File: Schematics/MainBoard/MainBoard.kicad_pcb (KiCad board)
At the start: 6 copper layers, 299.7 x 299.7 mm, 200 parts, among them J1 Barrel_Jack, J10 ALU Result LED Connector, J11 Address Bus LED Connector, J12 Data Bus LED Connector, J13 PC/IF Connector [0..7], J14 PC/IF Connector [8..15], J15 IROM Connector [0..7], J16 IROM Connector [8..15], J2 Device Select LED Connector, J3 Program Counter LED Connector, J4 Instruction Register LED Conn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, J5 C Register LED Connector, J6 Control Word LED Connector, J7 Speed Control LED Connector, J8 A Register LED Connector, J9 B Register LED Connector, SW1 Step, SW2 Reset, U1 74LS393, U10 IDT71256SA12TPG, U11 IDT71256SA12TPG, U12 74F377, U13 74LS138, U14 74F377, U15 74F377, U16 74LS245, U17 74LS245, U18 74F161, U19 74F161, U2 74LS32, U20 74F161, U21 74F161, U22 74F574, U23 74F574, U26 74F157, U27 74F157, U28 74F157, U29 74F157, U3 74F377, U30 74LS08, U31 74LS04, U32 74LS32, U33 IDT71256SA12TPG, U34 IDT71256SA12TPG, U35 74LS245, U36 74LS245, U37 74F157, U38 74F157, U39 74F574, U4 74LS139, U40 74F157, U41 74F157, U42 74F574, U43 GLS29EE010, U44 GLS29EE010, U45 74F574, U46 74F574, U47 74F574, U48 74LS245, U49 LM393, U5 74LS245, U50 LM393, U51 GLS29EE010, U52 LM393, U53 LM393, U54 74LS04, U55 LM555, U56 74LS393, U57 74LS151, U58 74LS393, U59 74LS393, U6 GLS29EE010, U60 LM555, U61 MCP100-450D, U62 74LS04, U63 74LS08, U64 74LS157, U65 74F377, U66 74LS245, U67 74F377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

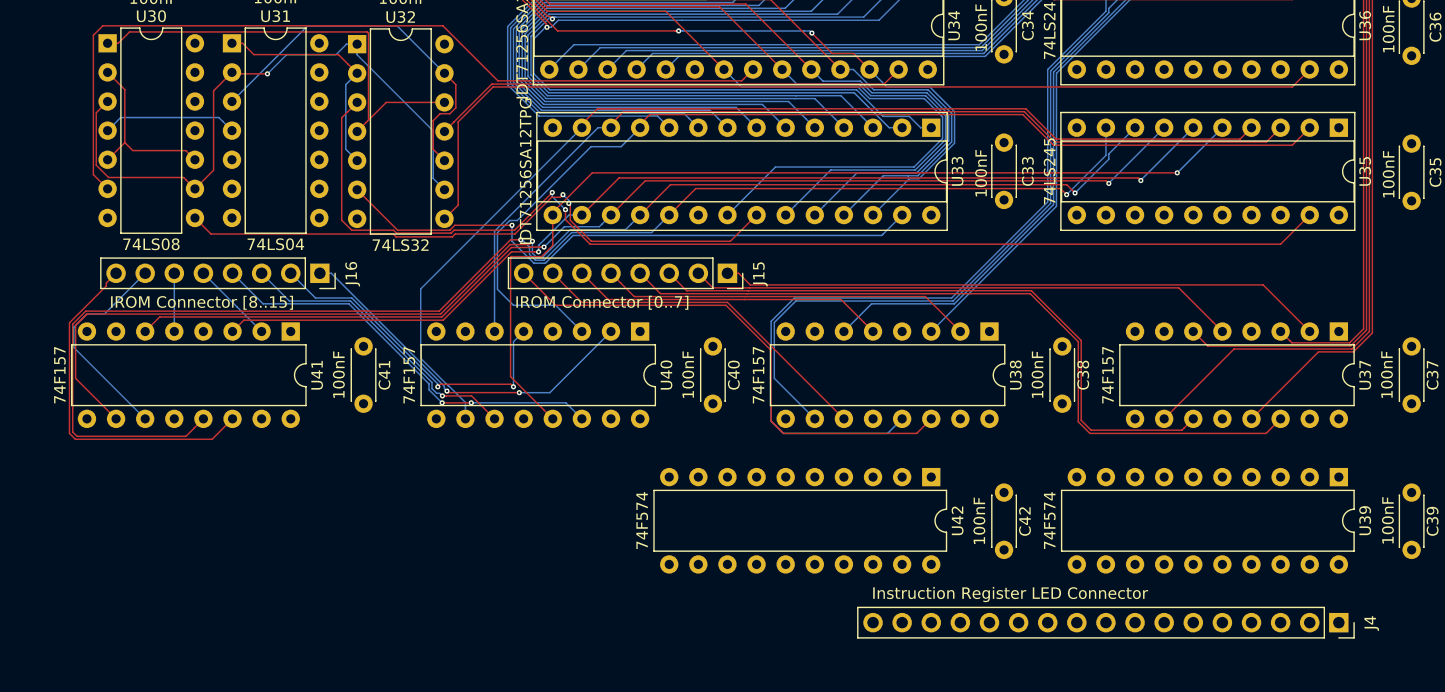
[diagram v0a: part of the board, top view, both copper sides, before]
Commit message: checkpoint: route up through the Instruction Register
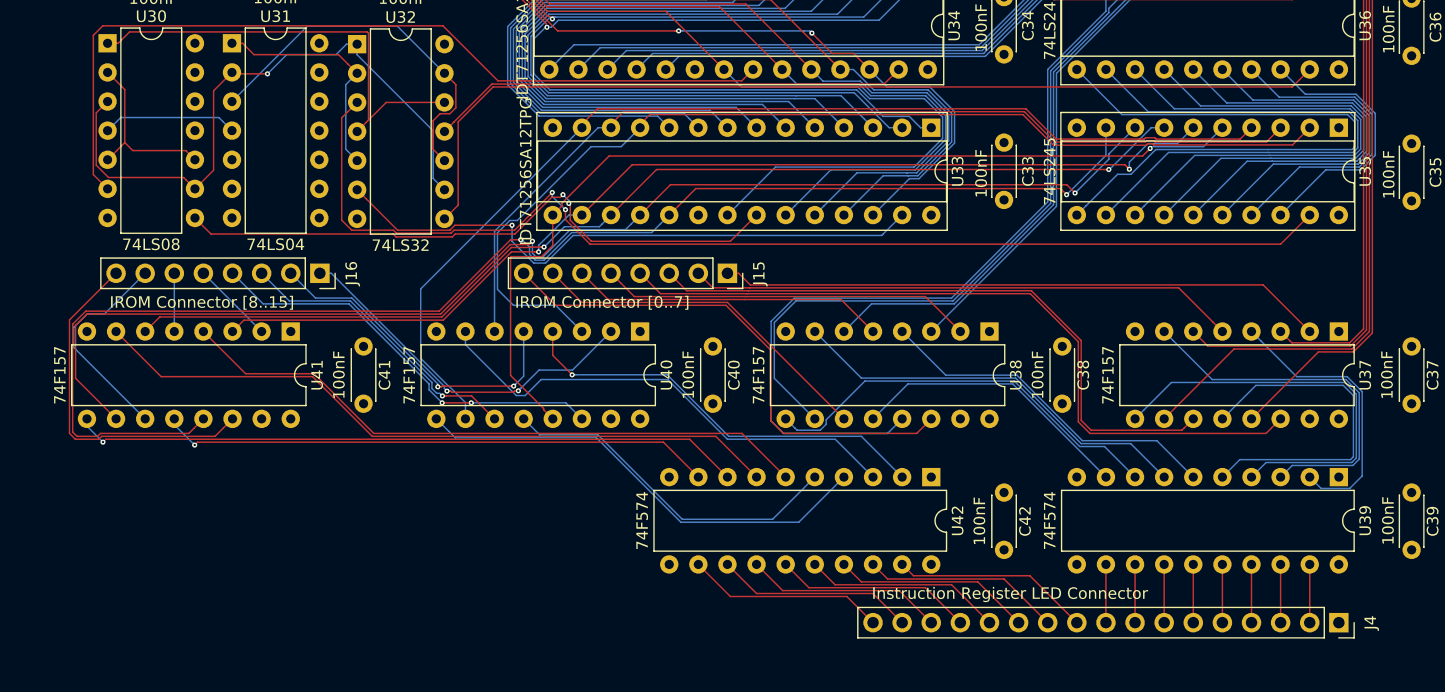
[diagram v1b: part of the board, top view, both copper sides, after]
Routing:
- net Net-(U41-Pad7): track 0.00 -> 61.1 mm
- net Net-(U41-Pad9): track 0.00 -> 58.6 mm, vias 0 -> 1
- net Net-(U41-Pad4): track 0.00 -> 56.1 mm
- net DataBus7: track 0.00 -> 55.0 mm
- net DataBus6: track 0.00 -> 50.6 mm
- net Net-(U41-Pad12): track 0.00 -> 48.3 mm, vias 0 -> 1
- net DataBus5: track 0.00 -> 46.1 mm
- net Net-(U40-Pad7): track 0.00 -> 42.6 mm
- net DataBus4: track 0.00 -> 41.7 mm
- net Net-(U40-Pad9): track 0.00 -> 40.9 mm
- net DataBus3: track 0.00 -> 37.2 mm
- net Net-(U40-Pad4): track 0.00 -> 37.0 mm, vias 0 -> 1
- net Net-(U37-Pad9): track 0.00 -> 36.4 mm
- net Net-(U38-Pad9): track 0.00 -> 36.4 mm
- net Net-(U38-Pad7): track 0.00 -> 35.7 mm
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
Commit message: stake out a place for the Program Counter ICs.
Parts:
- moved J3 325.3 mm to (309.9, 109.2), turned to 270 degrees
- moved U18 312.3 mm to (309.9, 96.5), turned to 270 degrees
- moved U19 299.0 mm to (279.4, 96.5), turned to 270 degrees
- moved C18 293.2 mm to (316.2, 97.8), turned to 270 degrees
- moved U20 291.0 mm to (248.9, 96.5), turned to 270 degrees
- moved U21 288.8 mm to (218.4, 96.5), turned to 270 degrees
- moved C19 279.7 mm to (285.8, 97.8), turned to 270 degrees
- moved C21 275.6 mm to (224.8, 102.9), turned to 90 degrees
- moved C20 274.3 mm to (255.3, 97.8), turned to 270 degrees

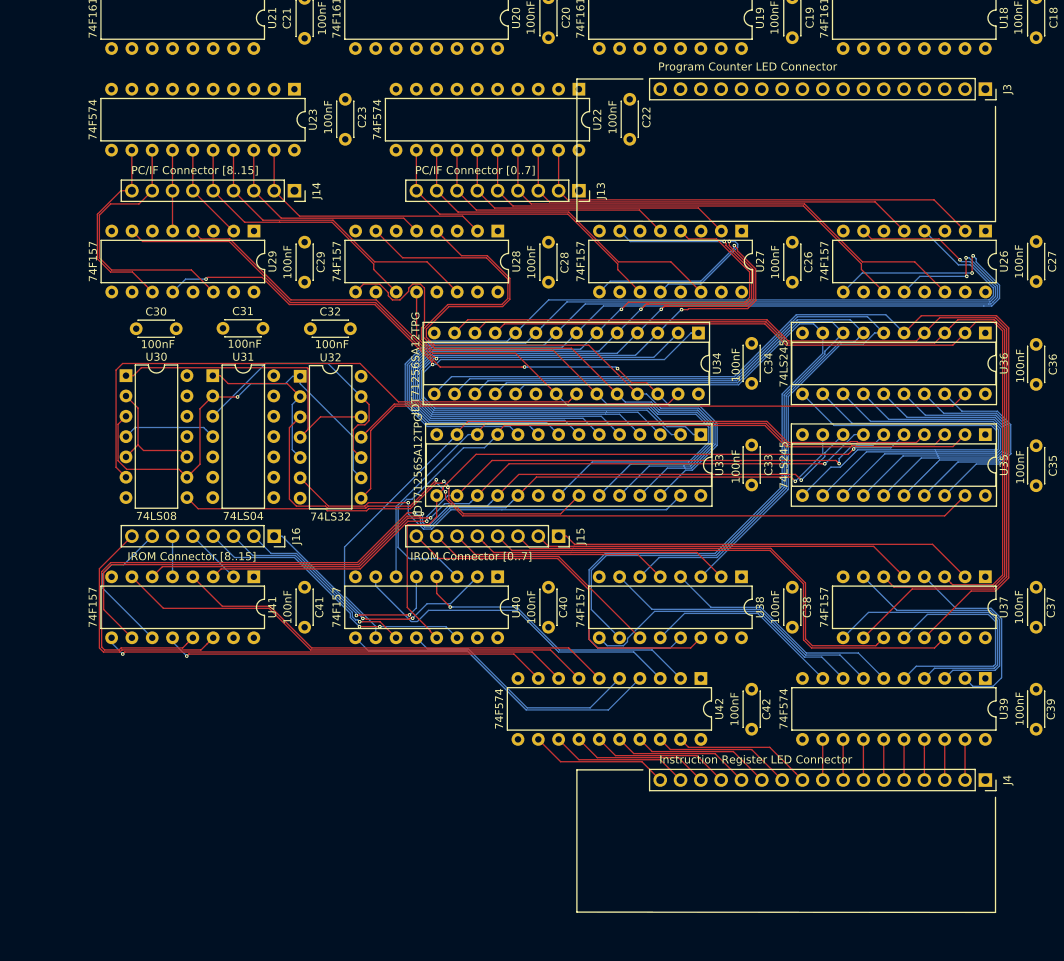
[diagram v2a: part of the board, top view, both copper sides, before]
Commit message: Route connection between PC and PC/IF.
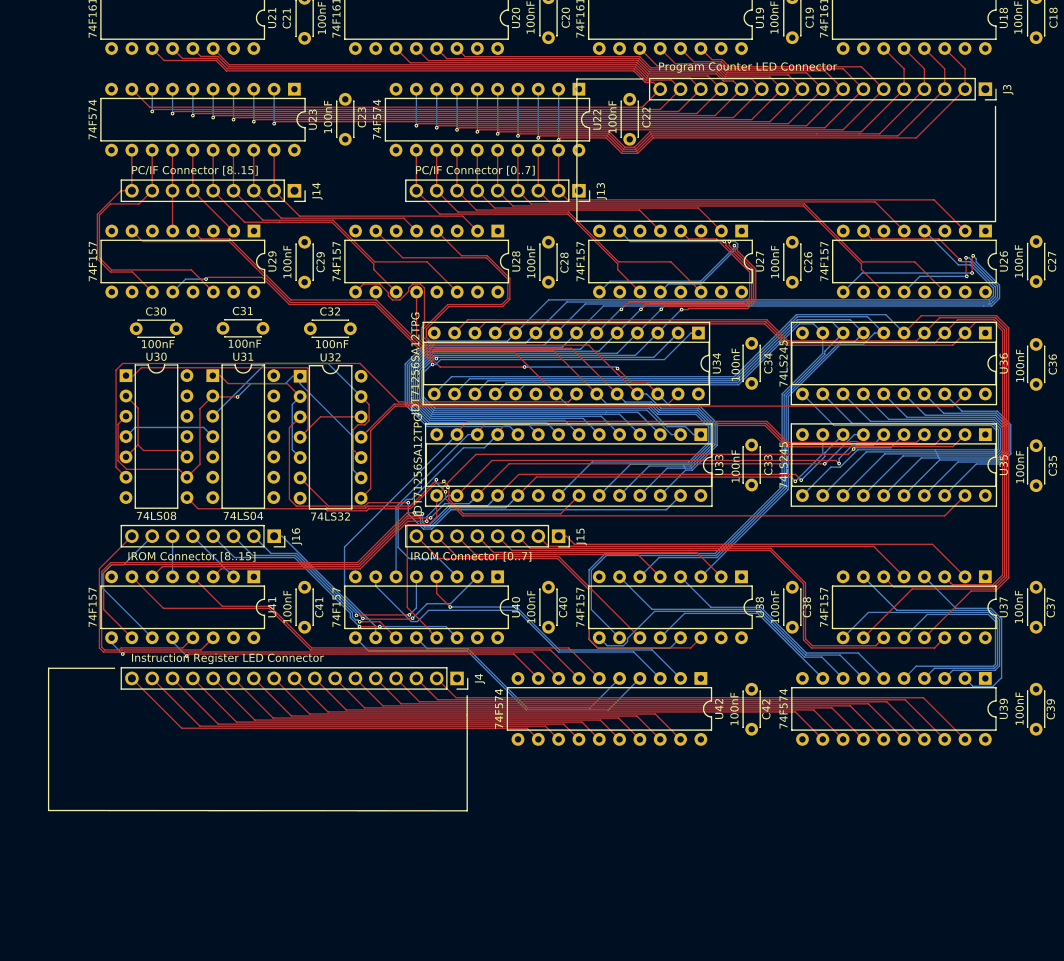
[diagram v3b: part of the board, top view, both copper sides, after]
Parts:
- moved J4 67.3 mm to (243.8, 182.9)
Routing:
- net PC12: track 0.00 -> 136.3 mm, vias 0 -> 1
- net PC13: track 0.00 -> 136.0 mm, vias 0 -> 1
- net PC14: track 0.00 -> 135.6 mm, vias 0 -> 1
- net PC15: track 0.00 -> 133.5 mm
- net PC8: track 0.00 -> 117.4 mm, vias 0 -> 1
- net PC9: track 0.00 -> 117.1 mm, vias 0 -> 1
- net PC10: track 0.00 -> 116.7 mm, vias 0 -> 1
- net PC11: track 0.00 -> 116.3 mm, vias 0 -> 1
- net PC4: track 0.00 -> 83.3 mm, vias 0 -> 1
- net PC5: track 0.00 -> 82.9 mm, vias 0 -> 1
- net PC6: track 0.00 -> 82.6 mm, vias 0 -> 1
- net PC7: track 0.00 -> 82.2 mm, vias 0 -> 1
- net PC0: track 0.00 -> 67.5 mm, vias 0 -> 1
- net PC1: track 0.00 -> 67.1 mm, vias 0 -> 1
- net PC2: track 0.00 -> 66.8 mm, vias 0 -> 1
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
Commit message: Stake out positions for the X and Y registers.
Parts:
- moved J11 319.2 mm to (243.8, 91.4), turned to 270 degrees
- moved C15 304.0 mm to (280.7, 85.1), turned to 270 degrees
- moved U15 300.2 mm to (274.3, 83.8), turned to 270 degrees
- moved U17 297.5 mm to (287.0, 91.4), turned to 90 degrees
- moved C14 295.5 mm to (280.7, 72.4), turned to 270 degrees
- moved U14 292.3 mm to (274.3, 71.1), turned to 270 degrees
- moved U16 288.1 mm to (287.0, 78.7), turned to 90 degrees
- moved C17 285.6 mm to (316.2, 85.1), turned to 270 degrees
- moved C16 276.8 mm to (316.2, 72.4), turned to 270 degrees
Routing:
- net ~J: track 0.00 -> 94.0 mm
- net Net-(U20-Pad15): track 0.00 -> 44.3 mm
- net Net-(U18-Pad15): track 0.00 -> 44.3 mm

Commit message: Stake out positions for register D and Device Select.
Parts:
- moved J2 265.2 mm to (243.8, 71.1), turned to 270 degrees
- moved C13 250.6 mm to (280.7, 64.8), turned to 90 degrees
- moved U13 242.7 mm to (274.3, 58.4), turned to 270 degrees
- moved U12 228.0 mm to (309.9, 58.4), turned to 270 degrees
- moved C12 211.0 mm to (316.2, 64.8), turned to 90 degrees

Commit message: Add M3 mounting holes (grounded) at all four corners of the board.
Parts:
- added REF**: MountingHole_3.2mm_M3_Pad, MountingHole:MountingHole_3.2mm_M3_Pad, F.Cu at (142.2, 45.7)
- added REF**: MountingHole_3.2mm_M3_Pad, MountingHole:MountingHole_3.2mm_M3_Pad, F.Cu at (142.2, 335.3)
- added REF**: MountingHole_3.2mm_M3_Pad, MountingHole:MountingHole_3.2mm_M3_Pad, F.Cu at (431.8, 335.3)
- added REF**: MountingHole_3.2mm_M3_Pad, MountingHole:MountingHole_3.2mm_M3_Pad, F.Cu at (431.8, 45.7)
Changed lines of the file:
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@@
     (tracks 1412)
     (zones 0)
-    (modules 200)
+    (modules 204)
     (nets 306)
   )
@@
     (mod_text_size 1 1)
     (mod_text_width 0.15)
-    (pad_size 1.524 1.524)
-    (pad_drill 0.762)
+    (pad_size 6.4 6.4)
+    (pad_drill 3.200001)
     (pad_to_mask_clearance 0)
     (aux_axis_origin 0 0)
@@
     (add_net ~YO)
   )
+  (module MountingHole:MountingHole_3.2mm_M3_Pad locked (layer F.Cu)
+    (at 142.24 45.72)
+    (descr "Mounting Hole 3.2mm, M3")
+    (tags "mounting hole 3.2mm m3")
+    (attr virtual)
+    (fp_text reference REF** (at 0 -4.2) (layer F.SilkS) hide
+      (effects (font (size 1 1) (thickness 0.15)))
+    )
+    (fp_text value MountingHole_3.2mm_M3_Pad (at 0 4.2) (layer F.Fab)
+      (effects (font (size 1 1) (thickness 0.15)))
+    )
+    (fp_text user %R (at 0.3 0) (layer F.Fab)
+      (effects (font (size 1 1) (thickness 0.15)))
+    )
+    (fp_circle (center 0 0) (end 3.2 0) (layer Cmts.User) (width 0.15))
+    (fp_circle (center 0 0) (end 3.45 0) (layer F.CrtYd) (width 0.05))
+    (pad 1 thru_hole circle (at 0 0) (size 6.4 6.4) (drill 3.200001) (layers *.Cu *.Mask)
+      (net 1 GND))
+  )
+  (module MountingHole:MountingHole_3.2mm_M3_Pad locked (layer F.Cu)
+    (at 142.24 335.28)
+    (descr "Mounting Hole 3.2mm, M3")
+    (tags "mounting hole 3.2mm m3")
+    (attr virtual)
+    (fp_text reference REF** (at 0 -4.2) (layer F.SilkS) hide
+      (effects (font (size 1 1) (thickness 0.15)))
+    )
+    (fp_text value MountingHole_3.2mm_M3_Pad (at 0 4.2) (layer F.Fab)
+      (effects (font (size 1 1) (thickness 0.15)))
+    )
+    (fp_text user %R (at 0.3 0) (layer F.Fab)
+      (effects (font (size 1 1) (thickness 0.15)))
+    )
+    (fp_circle (center 0 0) (end 3.2 0) (layer Cmts.User) (width 0.15))
+    (fp_circle (center 0 0) (end 3.45 0) (layer F.CrtYd) (width 0.05))
+    (pad 1 thru_hole circle (at 0 0) (size 6.4 6.4) (drill 3.200001) (layers *.Cu *.Mask)
+      (net 1 GND))
+  )
+  (module MountingHole:MountingHole_3.2mm_M3_Pad locked (layer F.Cu)
+    (at 431.8 335.28)
+    (descr "Mounting Hole 3.2mm, M3")
+    (tags "mounting hole 3.2mm m3")
+    (attr virtual)
+    (fp_text reference REF** (at 0 -4.2) (layer F.SilkS) hide
+      (effects (font (size 1 1) (thickness 0.15)))
+    )
+    (fp_text value MountingHole_3.2mm_M3_Pad (at 0 4.2) (layer F.Fab)
+      (effects (font (size 1 1) (thickness 0.15)))
+    )
+    (fp_text user %R (at 0.3 0) (layer F.Fab)
+      (effects (font (size 1 1) (thickness 0.15)))
+    )
+    (fp_circle (center 0 0) (end 3.2 0) (layer Cmts.User) (width 0.15))
+    (fp_circle (center 0 0) (end 3.45 0) (layer F.CrtYd) (width 0.05))
+    (pad 1 thru_hole circle (at 0 0) (size 6.4 6.4) (drill 3.200001) (layers *.Cu *.Mask)
+      (net 1 GND))
+  )
+  (module MountingHole:MountingHole_3.2mm_M3_Pad locked (layer F.Cu)
+    (at 431.8 45.72)
+    (descr "Mounting Hole 3.2mm, M3")
+    (tags "mounting hole 3.2mm m3")
+    (attr virtual)
+    (fp_text reference REF** (at 0 -4.2) (layer F.SilkS) hide
+      (effects (font (size 1 1) (thickness 0.15)))
+    )
+    (fp_text value MountingHole_3.2mm_M3_Pad (at 0 4.2) (layer F.Fab)
+      (effects (font (size 1 1) (thickness 0.15)))
+    )
+    (fp_circle (center 0 0) (end 3.45 0) (layer F.CrtYd) (width 0.05))
+    (fp_circle (center 0 0) (end 3.2 0) (layer Cmts.User) (width 0.15))
+    (fp_text user %R (at 0.3 0) (layer F.Fab)
+      (effects (font (size 1 1) (thickness 0.15)))
+    )
+    (pad 1 thru_hole circle (at 0 0) (size 6.4 6.4) (drill 3.200001) (layers *.Cu *.Mask)
+      (net 1 GND))
+  )
   (module Connector_PinSocket_2.54mm:PinSocket_1x08_P2.54mm_Vertical (layer F.Cu)

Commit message: Route lines for the address bus out of XY and into Instruction RAM.
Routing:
- net AddressBus0: track 0.00 -> 249.8 mm
- net AddressBus2: track 0.00 -> 247.6 mm, vias 0 -> 1
- net AddressBus1: track 0.00 -> 240.3 mm
- net AddressBus3: track 0.00 -> 238.6 mm, vias 0 -> 1
- net AddressBus4: track 0.00 -> 210.2 mm
- net AddressBus6: track 0.00 -> 207.3 mm, vias 0 -> 1
- net AddressBus5: track 0.00 -> 200.7 mm
- net AddressBus7: track 0.00 -> 198.4 mm, vias 0 -> 1
- net AddressBus8: track 0.00 -> 166.0 mm
- net AddressBus10: track 0.00 -> 157.8 mm
- net AddressBus9: track 0.00 -> 151.5 mm
- net AddressBus11: track 0.00 -> 148.9 mm
- net AddressBus15: track 0.00 -> 133.4 mm, vias 0 -> 1
- net AddressBus14: track 0.00 -> 132.6 mm, vias 0 -> 1
- net AddressBus13: track 0.00 -> 122.8 mm, vias 0 -> 3
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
